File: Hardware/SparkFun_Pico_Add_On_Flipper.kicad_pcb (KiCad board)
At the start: 2 copper layers, 25.4 x 50.8 mm, 106 parts, among them J1 Conn_01x20, J2 Conn_01x20, J3 Conn_01x20, J4 Conn_01x20, J5 Qwiic_RA, SW1 SMD_RA_5x3mm_h3.6mm

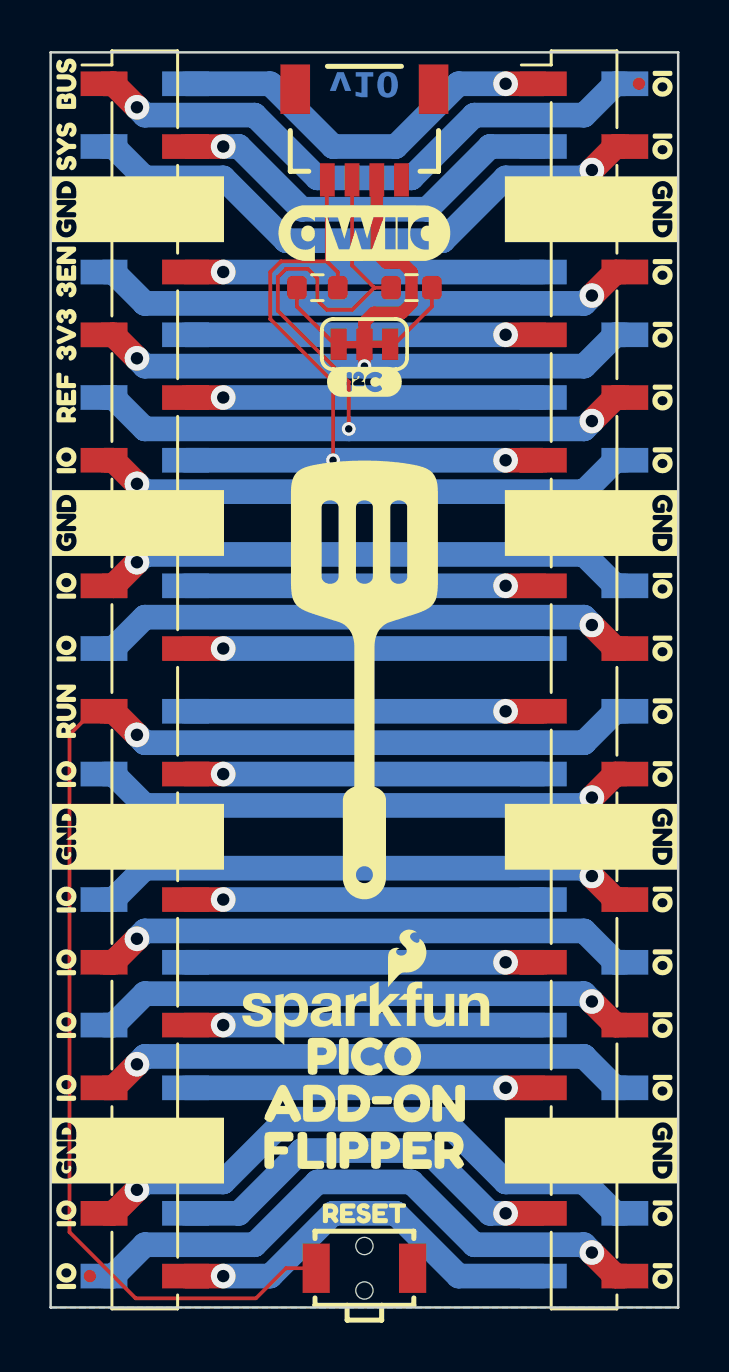
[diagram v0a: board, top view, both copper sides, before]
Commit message: Design Review Updates
Widen pads of 1x20 headers
Add "Analog" silk label to ADC pins
Rotate pin labels 180 degrees (more readable when viewing from outside)
Fill out title blocks of schematic and board
Widen traces to 0.01"
Set board constraints, 0.005" copper clearance
Shrink product name in silk and update capitalization
Update ordering notes
Add reset button silk to bottom
Exclude irrelevant DRC warnings/errors
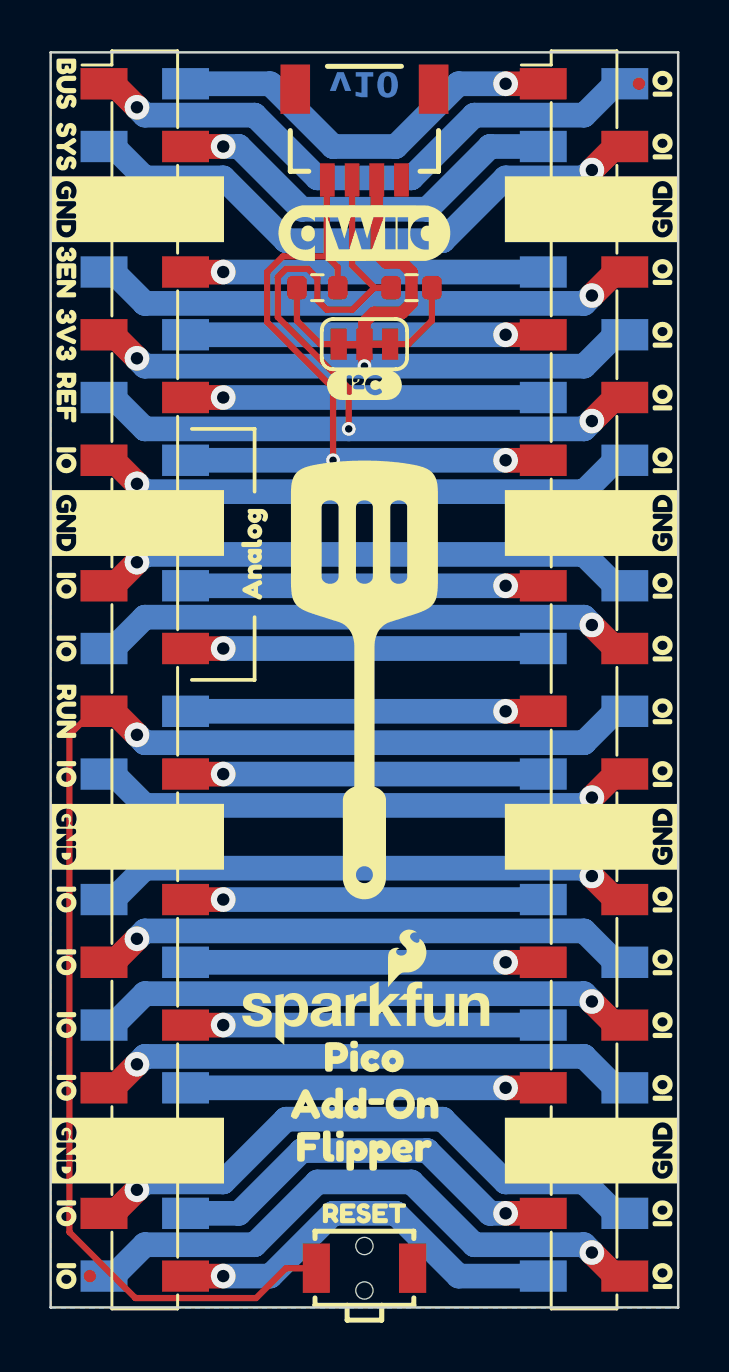
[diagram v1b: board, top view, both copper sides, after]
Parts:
- removed kibuzzard-67A3A70A (x2): G***, kibuzzard-67A3A70A
- removed kibuzzard-67ABB6D6 (x2): G***, kibuzzard-67ABB6D6
- removed kibuzzard-67ABB6DB (x2): G***, kibuzzard-67ABB6DB
- added kibuzzard-67ABB6E7: G***, kibuzzard-67ABB6E7, B.Cu at (128.3, 122.9)
- added kibuzzard-67AE6710: G***, kibuzzard-67AE6710, F.Cu at (123.8, 94.0)
- added kibuzzard-67AE6710: G***, kibuzzard-67AE6710, B.Cu at (132.7, 94.0)
- added kibuzzard-67AE711B: G***, kibuzzard-67AE711B, F.Cu at (128.3, 118.1)
- added kibuzzard-67AE711B: G***, kibuzzard-67AE711B, B.Cu at (128.3, 118.1)
- added kibuzzard-67AE7122: G***, kibuzzard-67AE7122, F.Cu at (128.3, 116.2)
- added kibuzzard-67AE7122: G***, kibuzzard-67AE7122, B.Cu at (128.3, 116.2)
- added kibuzzard-67AE7131: G***, kibuzzard-67AE7131, F.Cu at (128.3, 114.3)
- added kibuzzard-67AE7131: G***, kibuzzard-67AE7131, B.Cu at (128.3, 114.3)
- JP1: value ~ -> I2C
- moved kibuzzard-67A3AA74 0.13 mm to (128.3, 87.1)
- turned kibuzzard-67A3A1F6 to -90 degrees (x2)
- turned kibuzzard-67A3A2B7 to -90 degrees (x2)
- turned kibuzzard-67A3A2E9 to -90 degrees (x2)
- turned kibuzzard-67A3A308 to -90 degrees (x2)
- turned kibuzzard-67A3A314 to -90 degrees (x2)
- turned kibuzzard-67A3A317 to -90 degrees (x2)
- turned kibuzzard-67ABBF88 to -90 degrees
- turned kibuzzard-67ABBF88 to 90 degrees
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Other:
- board text added: "Finish: Lead-Free HASL"
- board text added: "Layers: 2"
- board text added: "Material: TG135"
- board text removed: "Controlled Impedance: JLC7628"
- board text removed: "Finish: ENIG"
- board text removed: "Inner Copper Weight: 0.5oz"
- board text removed: "Layers: 4"
- board text removed: "Material: TG155"
- board text removed: "No Clean Process"

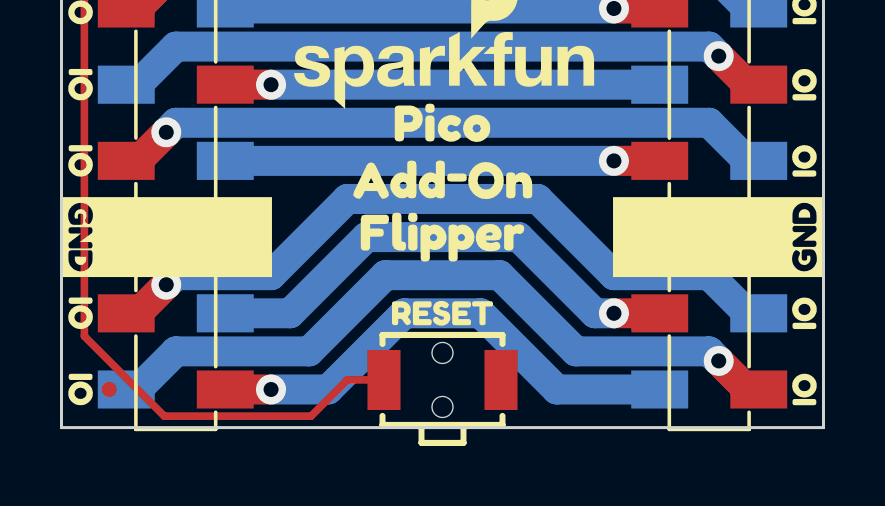
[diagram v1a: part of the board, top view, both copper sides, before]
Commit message: Change reset button
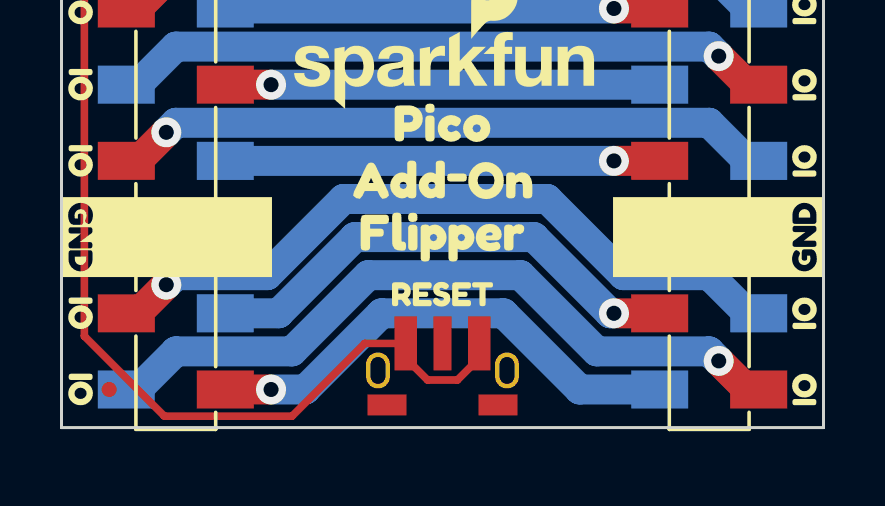
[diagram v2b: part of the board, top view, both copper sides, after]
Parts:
- SW1: footprint SparkFun-Switch:Push_SMD_RA_5x3mm -> SparkFun-Switch:Push_SMD_RA_4.5x2.5mm
- moved kibuzzard-67ABB6E7 0.95 mm to (128.3, 123.8)
- moved kibuzzard-67ABB6E7 0.64 mm to (128.3, 120.0)
- moved SW1 0.32 mm to (128.3, 122.6)
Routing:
- net RUN: track 55.6 -> 60.9 mm

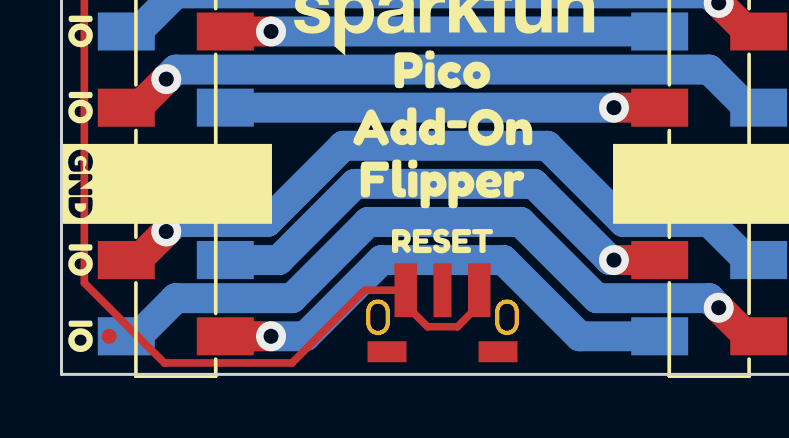
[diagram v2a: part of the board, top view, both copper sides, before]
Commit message: Change reset button
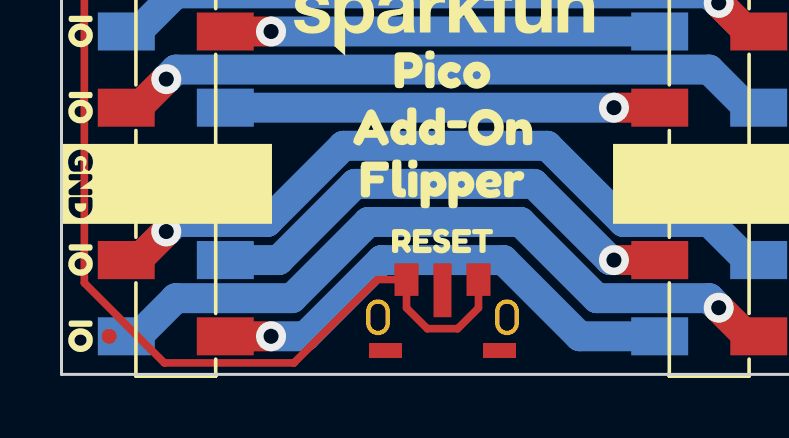
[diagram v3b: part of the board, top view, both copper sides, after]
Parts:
- J5: footprint SparkFun-Connector:JST_SMD_1.0mm-4_RA -> SparkFun-Connector:JST_SMD_1.0mm-4_Black
- SW1: footprint SparkFun-Switch:Push_SMD_RA_4.5x2.5mm -> SparkFun-Switch:Push_SMD_RA_4.5x3.4mm
- turned SW1 to 180 degrees
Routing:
- net RUN: track 60.9 -> 61.9 mm

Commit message: Update 1x20 header
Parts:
- J1, J2, J3, J4: footprint SparkFun-Connector:1x20_SMD_Pin1Left_Passthru -> SparkFun-Connector:1x20_SMD_Pin1RightUp
- turned J1 to 90 degrees
- turned J2 to 90 degrees
- turned J3 to 90 degrees
- turned J4 to 90 degrees

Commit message: Tweak routing
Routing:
- net IO15: track 24.2 -> 23.7 mm
- net VSYS: track 16.6 -> 16.1 mm
- net IO14: track 16.6 -> 16.1 mm
- net IO0: track 16.6 -> 16.1 mm
- net IO1: track 24.2 -> 23.7 mm
- net VBUS: track 24.2 -> 23.7 mm
- net IO17: track 24.2 -> 23.7 mm
- net IO16: track 16.6 -> 16.1 mm
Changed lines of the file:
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@@
 	)
 	(segment
-		(start 133.985 78.74)
-		(end 131.445 81.28)
+		(start 137.16 78.74)
+		(end 133.985 78.74)
 		(width 1)
 		(layer "B.Cu")
@@
 	)
 	(segment
-		(start 125.095 81.28)
+		(start 122.555 78.74)
+		(end 119.38 78.74)
+		(width 1)
+		(layer "B.Cu")
+		(net 14)
+	)
+	(segment
+		(start 133.985 78.74)
+		(end 132.08 80.645)
+		(width 1)
+		(layer "B.Cu")
+		(net 14)
+	)
+	(segment
+		(start 132.08 80.645)
+		(end 124.46 80.645)
+		(width 1)
+		(layer "B.Cu")
+		(net 14)
+	)
+	(segment
+		(start 124.46 80.645)
 		(end 122.555 78.74)
 		(width 1)
@@
 	)
 	(segment
-		(start 137.16 78.74)
-		(end 133.985 78.74)
-		(width 1)
-		(layer "B.Cu")
-		(net 14)
-	)
-	(segment
-		(start 122.555 78.74)
-		(end 119.38 78.74)
-		(width 1)
-		(layer "B.Cu")
-		(net 14)
-	)
-	(segment
 		(start 118.11 77.47)
 		(end 117.73 77.47)
@@
 	)
 	(segment
-		(start 131.445 81.28)
-		(end 125.095 81.28)
-		(width 1)
-		(layer "B.Cu")
-		(net 14)
-	)
-	(segment
 		(start 138.43 102.87)
 		(end 138.81 102.87)
@@
 	)
 	(segment
-		(start 127 77.47)
-		(end 124.46 74.93)
+		(start 124.46 74.93)
+		(end 121.03 74.93)
 		(width 1)
 		(layer "B.Cu")
@@
 	)
 	(segment
+		(start 130.175 76.835)
+		(end 126.365 76.835)
+		(width 1)
+		(layer "B.Cu")
+		(net 18)
+	)
+	(segment
 		(start 132.08 74.93)
-		(end 129.54 77.47)
+		(end 130.175 76.835)
 		(width 1)
 		(layer "B.Cu")
@@
 	)
 	(segment
-		(start 124.46 74.93)
-		(end 121.03 74.93)
-		(width 1)
-		(layer "B.Cu")
-		(net 18)
-	)
-	(segment
-		(start 129.54 77.47)
-		(end 127 77.47)
+		(start 126.365 76.835)
+		(end 124.46 74.93)
 		(width 1)
 		(layer "B.Cu")
@@
 	)
 	(segment
-		(start 126.238 120.65)
-		(end 130.302 120.65)
+		(start 123.237625 123.19)
+		(end 125.142625 121.285)
 		(width 1)
 		(layer "B.Cu")
@@
 	)
 	(segment
-		(start 130.302 120.65)
-		(end 132.842 123.19)
+		(start 131.426046 121.285)
+		(end 133.331046 123.19)
 		(width 1)
 		(layer "B.Cu")
@@
 	)
 	(segment
+		(start 125.142625 121.285)
+		(end 131.426046 121.285)
+		(width 1)
+		(layer "B.Cu")
+		(net 22)
+	)
+	(segment
 		(start 122.555 123.19)
-		(end 123.698 123.19)
+		(end 123.237625 123.19)
 		(width 1)
 		(layer "B.Cu")
@@
 	)
 	(segment
-		(start 132.842 123.19)
+		(start 133.331046 123.19)
 		(end 135.51 123.19)
-		(width 1)
-		(layer "B.Cu")
-		(net 22)
-	)
-	(segment
-		(start 123.698 123.19)
-		(end 126.238 120.65)
 		(width 1)
 		(layer "B.Cu")
@@
 	)
 	(segment
-		(start 130.175 78.74)
+		(start 123.825 76.2)
+		(end 125.73 78.105)
+		(width 1)
+		(layer "B.Cu")
+		(net 28)
+	)
+	(segment
+		(start 138.43 74.93)
+		(end 138.81 74.93)
+		(width 1)
+		(layer "B.Cu")
+		(net 28)
+	)
+	(segment
+		(start 130.81 78.105)
 		(end 132.715 76.2)
+		(width 1)
+		(layer "B.Cu")
+		(net 28)
+	)
+	(segment
+		(start 119.0625 75.8825)
+		(end 119.38 76.2)
 		(width 1)
 		(layer "B.Cu")
@@
 	)
 	(segment
-		(start 119.0625 75.8825)
-		(end 119.38 76.2)
+		(start 125.73 78.105)
+		(end 130.81 78.105)
+		(width 1)
+		(layer "B.Cu")
+		(net 28)
+	)
+	(segment
+		(start 132.715 76.2)
+		(end 137.16 76.2)
 		(width 1)
 		(layer "B.Cu")
@@
 	)
 	(segment
-		(start 132.715 76.2)
-		(end 137.16 76.2)
-		(width 1)
-		(layer "B.Cu")
-		(net 28)
-	)
-	(segment
-		(start 123.825 76.2)
-		(end 126.365 78.74)
-		(width 1)
-		(layer "B.Cu")
-		(net 28)
-	)
-	(segment
-		(start 126.365 78.74)
-		(end 130.175 78.74)
-		(width 1)
-		(layer "B.Cu")
-		(net 28)
-	)
-	(segment
-		(start 138.43 74.93)
-		(end 138.81 74.93)
-		(width 1)
-		(layer "B.Cu")
-		(net 28)
-	)
-	(segment
 		(start 118.11 120.65)
 		(end 117.73 120.65)
@@
 	)
 	(segment
-		(start 122.428 119.38)
-		(end 124.968 116.84)
+		(start 132.3975 117.475)
+		(end 134.3025 119.38)
+		(width 1)
+		(layer "B.Cu")
+		(net 29)
+	)
+	(segment
+		(start 119.0625 119.6975)
+		(end 119.38 119.38)
+		(width 1)
+		(layer "B.Cu")
+		(net 29)
+	)
+	(segment
+		(start 124.1425 117.475)
+		(end 132.3975 117.475)
+		(width 1)
+		(layer "B.Cu")
+		(net 29)
+	)
+	(segment
+		(start 119.38 119.38)
+		(end 122.2375 119.38)
+		(width 1)
+		(layer "B.Cu")
+		(net 29)
+	)
+	(segment
+		(start 138.43 120.65)
+		(end 138.81 120.65)
+		(width 1)
+		(layer "B.Cu")
+		(net 29)
+	)
+	(segment
+		(start 122.2375 119.38)
+		(end 124.1425 117.475)
 		(width 1)
 		(layer "B.Cu")
@@
 	)
 	(segment
-		(start 119.38 119.38)
-		(end 122.428 119.38)
-		(width 1)
-		(layer "B.Cu")
-		(net 29)
-	)
-	(segment
-		(start 124.968 116.84)
-		(end 131.7625 116.84)
-		(width 1)
-		(layer "B.Cu")
-		(net 29)
-	)
-	(segment
-		(start 119.0625 119.6975)
-		(end 119.38 119.38)
-		(width 1)
-		(layer "B.Cu")
-		(net 29)
-	)
-	(segment
-		(start 131.7625 116.84)
-		(end 134.3025 119.38)
-		(width 1)
-		(layer "B.Cu")
-		(net 29)
-	)
-	(segment
-		(start 138.43 120.65)
-		(end 138.81 120.65)
-		(width 1)
-		(layer "B.Cu")
-		(net 29)
-	)
-	(segment
 		(start 119.0625 109.5375)
 		(end 118.11 110.49)
@@
 	(segment
 		(start 133.35 77.47)
-		(end 130.81 80.01)
+		(end 131.445 79.375)
+		(width 1)
+		(layer "B.Cu")
+		(net 32)
+	)
+	(segment
+		(start 131.445 79.375)
+		(end 125.095 79.375)
+		(width 1)
+		(layer "B.Cu")
+		(net 32)
+	)
+	(segment
+		(start 125.095 79.375)
+		(end 123.19 77.47)
 		(width 1)
 		(layer "B.Cu")
@@
 	)
 	(segment
-		(start 130.81 80.01)
-		(end 125.73 80.01)
-		(width 1)
-		(layer "B.Cu")
-		(net 32)
-	)
-	(segment
-		(start 125.73 80.01)
-		(end 123.19 77.47)
-		(width 1)
-		(layer "B.Cu")
-		(net 32)
-	)
-	(segment
 		(start 118.11 90.17)
 		(end 117.73 90.17)
@@
 	)
 	(segment
-		(start 122.809 120.65)
-		(end 125.349 118.11)
+		(start 124.466318 118.745)
+		(end 132.073682 118.745)
 		(width 1)
 		(layer "B.Cu")
@@
 	)
 	(segment
-		(start 133.858 120.65)
+		(start 133.978682 120.65)
 		(end 133.985 120.65)
 		(width 1)
@@
 	)
 	(segment
-		(start 125.349 118.11)
-		(end 131.318 118.11)
+		(start 122.561318 120.65)
+		(end 124.466318 118.745)
 		(width 1)
 		(layer "B.Cu")
@@
 	(segment
 		(start 121.03 120.65)
-		(end 122.809 120.65)
+		(end 122.561318 120.65)
 		(width 1)
 		(layer "B.Cu")
@@
 	)
 	(segment
-		(start 131.318 118.11)
-		(end 133.858 120.65)
+		(start 132.073682 118.745)
+		(end 133.978682 120.65)
 		(width 1)
 		(layer "B.Cu")
@@
 	)
 	(segment
-		(start 125.7935 119.38)
-		(end 123.2535 121.92)
+		(start 137.16 121.92)
+		(end 133.654864 121.92)
 		(width 1)
 		(layer "B.Cu")
@@
 	)
 	(segment
-		(start 137.16 121.92)
-		(end 133.4135 121.92)
+		(start 133.654864 121.92)
+		(end 131.749864 120.015)
 		(width 1)
 		(layer "B.Cu")
@@
 	)
 	(segment
-		(start 119.38 121.92)
-		(end 118.11 123.19)
+		(start 122.885136 121.92)
+		(end 119 121.92)
 		(width 1)
 		(layer "B.Cu")
@@
 	)
 	(segment
-		(start 123.2535 121.92)
-		(end 119.38 121.92)
-		(width 1)
-		(layer "B.Cu")
-		(net 37)
-	)
-	(segment
-		(start 130.8735 119.38)
-		(end 125.7935 119.38)
-		(width 1)
-		(layer "B.Cu")
-		(net 37)
-	)
-	(segment
-		(start 133.4135 121.92)
-		(end 130.8735 119.38)
+		(start 119 121.92)
+		(end 117.73 123.19)
 		(width 1)
 		(layer "B.Cu")
@@
 	)
 	(segment
-		(start 118.11 123.19)
-		(end 117.73 123.19)
-		(width 1)
-		(layer "B.Cu")
+		(start 131.749864 120.015)
+		(end 124.790136 120.015)
+		(width 1)
+		(layer "B.Cu")
+		(net 37)
+	)
+	(segment
+		(start 124.790136 120.015)
+		(end 122.885136 121.92)
+		(width 1)
+		(layer "B.Cu")

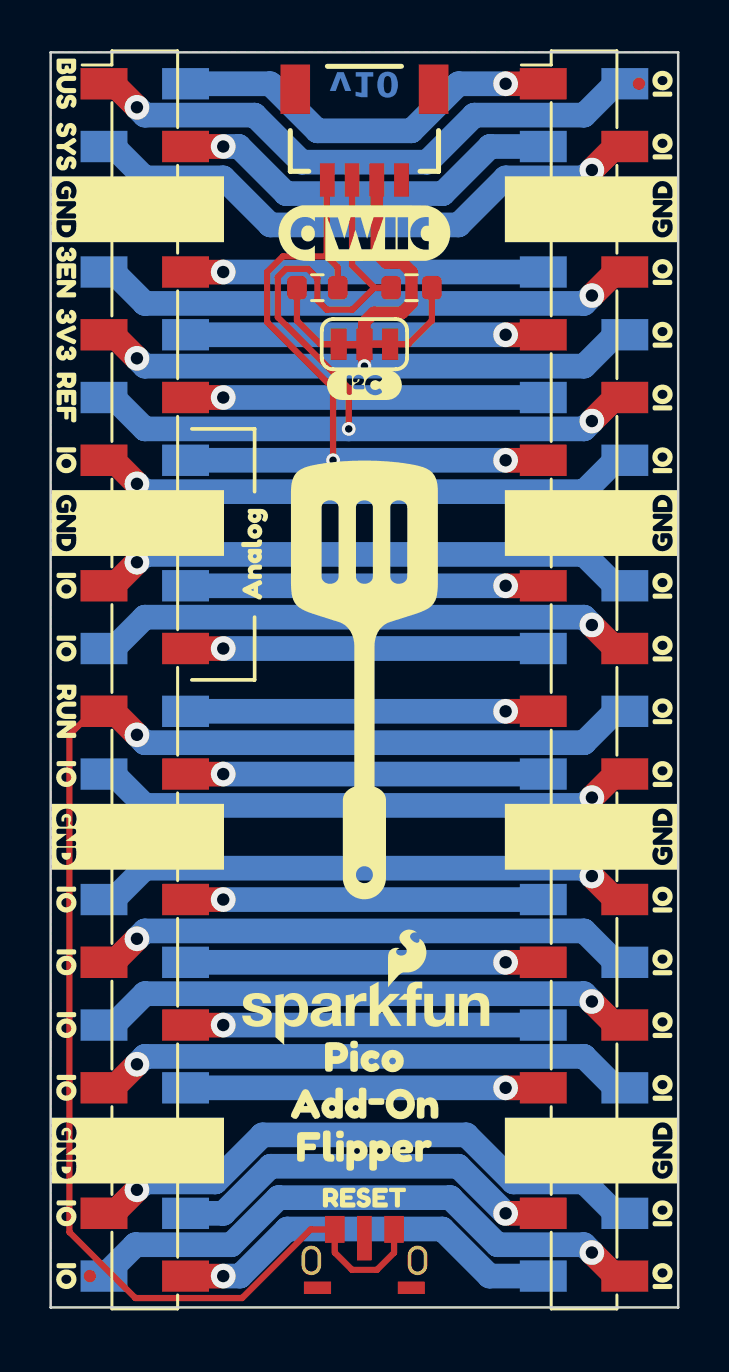
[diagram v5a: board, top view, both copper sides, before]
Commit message: Design Review Updates
Fix J1 text location in schematic
Organize ordering notes better
Shrink big vias to match small vias
Nudge button down 0.005"
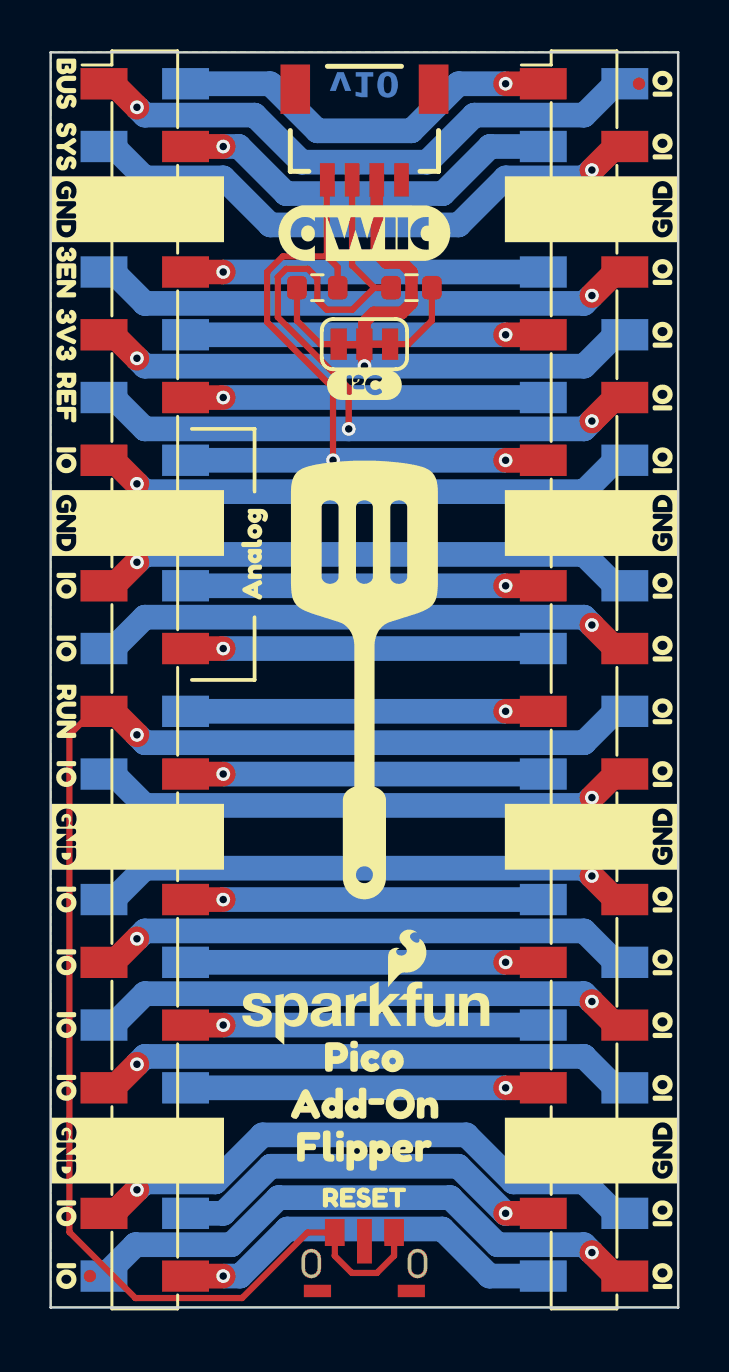
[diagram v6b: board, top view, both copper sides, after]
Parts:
- SW1: value SMD_RA_5x3mm_h3.6mm -> SMD_RA_4.5x3.4mm_h3.3mm
- moved SW1 0.13 mm to (128.3, 122.7)
